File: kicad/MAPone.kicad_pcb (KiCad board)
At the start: 2 copper layers, 0 parts

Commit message: MAPone schematic, work in progress
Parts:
- added C1: 100n, Capacitors_ThroughHole:Capacitor7x2RM5, F.Cu at (206.5, 134.9)
- added C2: 100u, Capacitors_ThroughHole:Capacitor5x6RM2.5, F.Cu at (207.7, 115.4)
- added C3: 100n, Capacitors_ThroughHole:Capacitor7x2RM5, F.Cu at (233.5, 119.8)
- added C4: 100n, Capacitors_ThroughHole:Capacitor7x2RM5, F.Cu at (214.8, 138.6)
- added C5: 100n, Capacitors_ThroughHole:Capacitor7x2RM5, F.Cu at (225.2, 119.8)
- added C6: 100n, Capacitors_ThroughHole:Capacitor7x2RM5, F.Cu at (214.8, 129.5)
- added D1: D_CPL, Diodes_ThroughHole:Diode_DO-35_SOD27_Horizontal_RM10, F.Cu at (171.2, 141.3)
- added D2: PWR, LEDs:LED-5MM, F.Cu at (205.6, 125.4)
- added D3: Blink, LEDs:LED-5MM, F.Cu at (180.7, 140.8)
- added H1: V_SEL, Pin_Headers:Pin_Header_Straight_1x03, F.Cu at (196.3, 140.2)
- added H2: Power, Pin_Headers:Pin_Header_Straight_1x07, F.Cu at (195.2, 118.6)
- added H4: ANALOG, Pin_Headers:Pin_Header_Straight_1x06, F.Cu at (172.9, 124.0)
- added H5: AREF, Pin_Headers:Pin_Header_Straight_1x03, F.Cu at (188.0, 140.2)
- added H6: IO_L, Pin_Headers:Pin_Header_Straight_1x08, F.Cu at (214.5, 108.2)
- added H7: IO_H, Pin_Headers:Pin_Header_Straight_1x08, F.Cu at (175.5, 118.6)
- added H8: FTDI, Pin_Headers:Pin_Header_Straight_1x06, F.Cu at (188.8, 124.0)
- added H9: ISP, Pin_Headers:Pin_Header_Straight_2x03, F.Cu at (223.2, 129.9)
- added R1: 10k, Resistors_ThroughHole:Resistor_Horizontal_RM10mm, F.Cu at (231.3, 109.8)
- added R2: 1k, Resistors_ThroughHole:Resistor_Horizontal_RM10mm, F.Cu at (184.0, 130.8)
- added R3: 1k, Resistors_ThroughHole:Resistor_Horizontal_RM10mm, F.Cu at (171.3, 130.8)
- added U1: 7805, Discret:LM78XXV, F.Cu at (215.7, 119.8)
- added U2: ATMEGA328-P, Sockets_DIP:DIP-28__300_ELL, F.Cu at (184.5, 109.7)
- added X1: 16MHz, Crystals:Crystal_HC49-U_Vertical_3Pin, F.Cu at (196.3, 131.2)

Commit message: MAPone schematic, work in progress
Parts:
- added C7: 22pF, Discret:C1, F.Cu at (98.0, 86.0)
- added C8: 22pF, Discret:C1, F.Cu at (92.0, 86.0)
- added J1: BARREL_JACK, uControl:JACK_ALIM, F.Cu at (60.0, 115.0)
- added J2: USB-Micro, BADGEr:USB_B_Micro, F.Cu at (56.0, 104.0)
- added P1: CONN_1, BADGEr:vite_3mm, F.Cu at (77.0, 76.0)
- added P2: CONN_1, BADGEr:vite_3mm, F.Cu at (133.0, 76.0)
- added P3: CONN_1, BADGEr:vite_3mm, F.Cu at (78.0, 120.0)
- added P4: CONN_1, BADGEr:vite_3mm, F.Cu at (134.0, 119.0)
- added SW1: RST, uControl:SW-PB, F.Cu at (126.0, 99.0)
- C2: footprint Capacitors_ThroughHole:Capacitor5x6RM2.5 -> Capacitors_Elko_ThroughHole:Elko_vert_11.2x6.3mm_RM2.5
- D1: value D_CPL -> 1N4007
- H7: footprint Pin_Headers:Pin_Header_Straight_1x08 -> Pin_Headers:Pin_Header_Straight_1x10
- H8: footprint Pin_Headers:Pin_Header_Straight_1x06 -> BADGEr:Header_FTDI
- H9: footprint Pin_Headers:Pin_Header_Straight_2x03 -> BADGEr:Header_ICSP
- moved C3 170.7 mm to (64.0, 100.0)
- moved U1 163.1 mm to (55.0, 92.0), turned to 180 degrees
- moved C4 151.2 mm to (71.0, 92.0), turned to 90 degrees
- moved D2 148.7 mm to (63.0, 83.0), turned to 180 degrees
- moved H1 143.6 mm to (61.0, 92.0), turned to 270 degrees
- moved C2 143.0 mm to (65.0, 106.0), turned to 180 degrees
- moved C5 126.3 mm to (99.0, 114.0)
- moved R2 123.3 mm to (67.0, 92.0), turned to 270 degrees
- moved R1 121.7 mm to (111.0, 91.0)
- moved C6 115.2 mm to (109.0, 84.0)
- moved C1 110.8 mm to (99.0, 108.0)
- moved X1 109.0 mm to (95.0, 91.0), turned to 180 degrees
- moved D1 103.6 mm to (71.0, 115.0), turned to 90 degrees
- moved D3 100.0 mm to (84.0, 115.0)
- moved H6 99.5 mm to (120.0, 77.0), turned to 180 degrees
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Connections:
- X1 pad 3: (no net) -> GND

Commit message: MAPone schematic, work in progress
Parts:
- added SHIELD**: ARDUINO_SHIELD, MAPone.pretty:ARDUINO_UNO_SHIELD_2_040pins, F.Cu at (67.0, 125.0)
- moved H2 77.0 mm to (179.0, 118.0)
- moved H4 77.0 mm to (199.0, 118.0)
- moved P3 77.0 mm to (155.0, 119.0)
- moved P4 77.0 mm to (211.0, 118.0)
- moved H6 68.4 mm to (188.0, 70.0)
- moved H7 68.4 mm to (164.0, 70.0)
- moved P1 68.4 mm to (145.0, 69.0)
- moved P2 68.4 mm to (201.0, 69.0)
- moved D2 42.1 mm to (93.0, 112.5), turned to 270 degrees
- moved R2 32.6 mm to (88.0, 117.0)
- moved U1 25.5 mm to (73.5, 74.5), turned to 270 degrees
- moved H1 18.2 mm to (78.0, 98.5)
- moved J2 15.1 mm to (71.0, 106.0)
- moved H9 13.7 mm to (132.5, 96.5), turned to 270 degrees
- moved J1 12.0 mm to (72.0, 116.0)
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
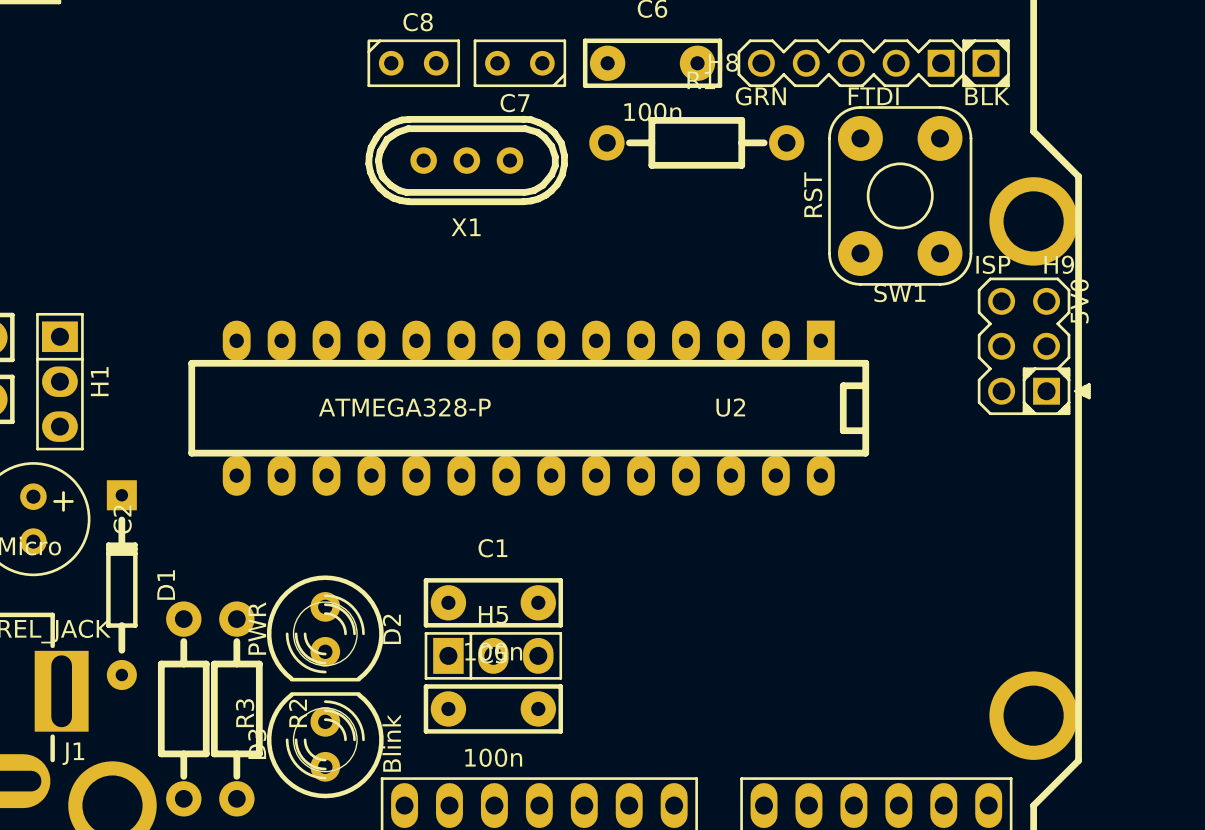
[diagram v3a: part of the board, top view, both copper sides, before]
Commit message: MAPone schematic review + PCB initialized
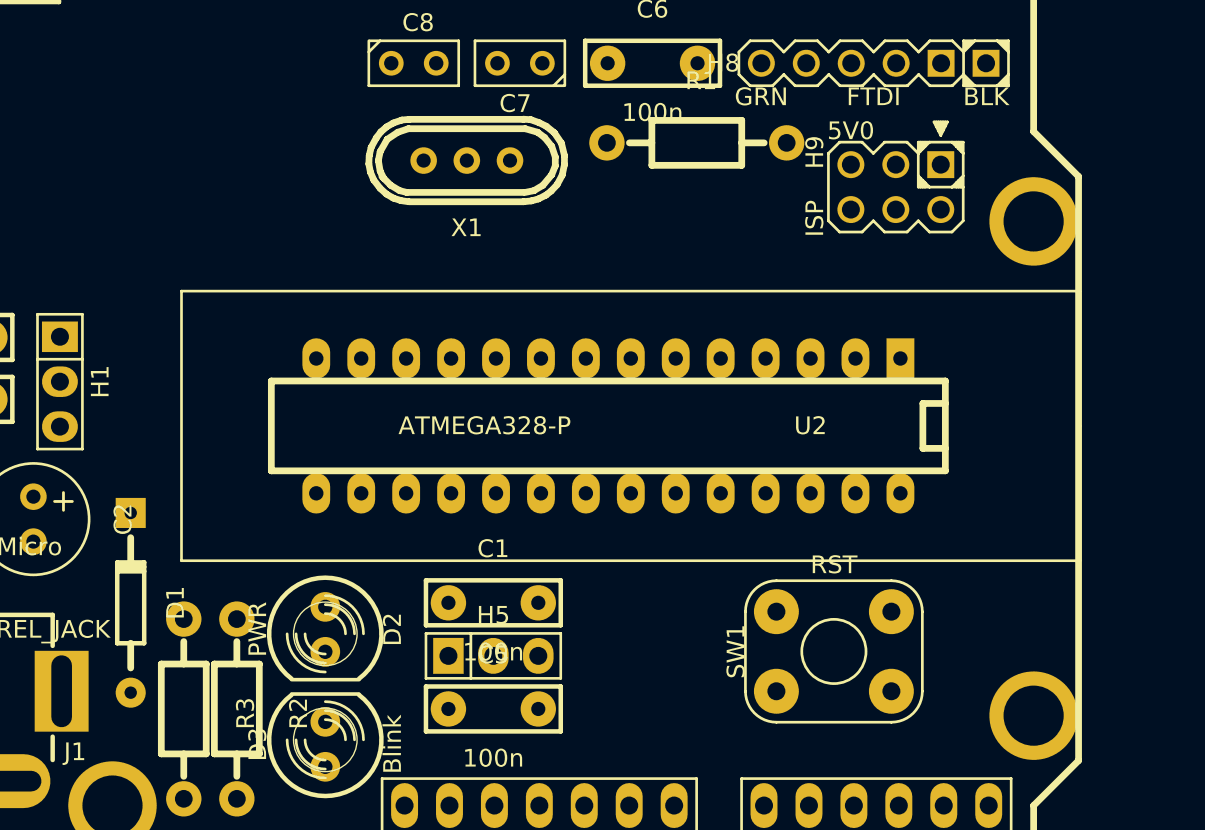
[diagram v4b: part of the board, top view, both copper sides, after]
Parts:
- U2: footprint Sockets_DIP:DIP-28__300_ELL -> MAPone.pretty:DIP-28__300_ELL_ZIF
- moved SW1 26.0 mm to (121.8, 113.8), turned to 90 degrees
- moved H9 11.6 mm to (125.2, 87.5), turned to 0 degrees
- moved U2 4.61 mm to (109.0, 101.0)
- moved D1 1.12 mm to (82.0, 111.0)

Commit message: MAPone PCB work in progress
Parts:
- removed P1, P2: CONN_1, BADGEr:vite_3mm
- removed SHIELD**: ARDUINO_SHIELD, MAPone.pretty:ARDUINO_UNO_SHIELD_2_040pins
- C1, C3, C4, C5, C6: footprint Capacitors_ThroughHole:Capacitor7x2RM5 -> MAPone.pretty:C_0805_HandSoldering; moved to B.Cu
- C2: footprint Capacitors_Elko_ThroughHole:Elko_vert_11.2x6.3mm_RM2.5 -> MAPone.pretty:Elko_vert_11.2x6.3mm_RM2.5
- C7, C8: footprint Discret:C1 -> MAPone.pretty:C_0805_HandSoldering; moved to B.Cu
- D1: footprint Diodes_ThroughHole:Diode_DO-35_SOD27_Horizontal_RM10 -> MAPone.pretty:Diode_DO-41_SOD81_Vertical_KathodeUp
- D2, D3: footprint LEDs:LED-5MM -> MAPone.pretty:LED-3MM
- H1: footprint Pin_Headers:Pin_Header_Straight_1x03 -> MAPone.pretty:Header_3
- H2: footprint Pin_Headers:Pin_Header_Straight_1x07 -> MAPone.pretty:Socket_Strip_Straight_1x06
- H4: footprint Pin_Headers:Pin_Header_Straight_1x06 -> MAPone.pretty:Socket_Strip_Straight_1x06
- H5: footprint Pin_Headers:Pin_Header_Straight_1x03 -> MAPone.pretty:Header_A_REF
- H6: footprint Pin_Headers:Pin_Header_Straight_1x08 -> MAPone.pretty:Socket_Strip_Straight_1x08
- H7: footprint Pin_Headers:Pin_Header_Straight_1x10 -> MAPone.pretty:Socket_Strip_Straight_1x08
- H8: footprint BADGEr:Header_FTDI -> MAPone.pretty:Header_FTDI
- H9: footprint BADGEr:Header_ICSP -> MAPone.pretty:Header_ICSP
- J1: footprint uControl:JACK_ALIM -> MAPone.pretty:JACK_ALIM
- J2: footprint BADGEr:USB_B_Micro -> MAPone.pretty:USB_B_Micro; moved to B.Cu
- P3, P4: footprint BADGEr:vite_3mm -> MAPone.pretty:vite_3mm
- R1, R2, R3: footprint Resistors_ThroughHole:Resistor_Horizontal_RM10mm -> MAPone.pretty:R_0805_HandSoldering; moved to B.Cu
- SW1: footprint uControl:SW-PB -> MAPone.pretty:SW-PB
- U1: footprint Discret:LM78XXV -> MAPone.pretty:LM78XXV
- X1: footprint Crystals:Crystal_HC49-U_Vertical_3Pin -> MAPone.pretty:Crystal_HC49-U_Vertical_3Pin
- moved H4 75.9 mm to (123.5, 110.0), turned to 180 degrees
- moved H2 73.6 mm to (105.8, 110.0)
- moved P3 71.4 mm to (84.0, 111.0)
- moved P4 71.3 mm to (140.0, 111.0)
- moved H6 68.6 mm to (121.0, 84.6), turned to 0 degrees
- moved H7 66.6 mm to (99.0, 84.6), turned to 180 degrees
- moved H9 32.6 mm to (92.7, 89.1)
- moved SW1 30.2 mm to (136.3, 87.3), turned to 270 degrees
- moved C6 27.8 mm to (131.3, 100.0)
- moved H5 27.8 mm to (114.6, 89.0)
- moved H8 25.2 mm to (140.0, 100.0), turned to 90 degrees
- moved C5 20.5 mm to (114.0, 100.0)
- moved C7 19.8 mm to (107.5, 100.0), turned to 0 degrees
- moved C8 19.8 mm to (101.3, 100.0), turned to 180 degrees
- moved R1 18.7 mm to (125.1, 100.1)
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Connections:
- H2 pad 1: /5V -> /RST
- H2 pad 2: /RST -> (no net)
- H2 pad 3: /3V3 -> /5V
- H2 pad 4: /5V -> GND
- H2 pad 6: GND -> /V_IN
- H8 pad 3: /V_USB -> /5V
- J1 pad 3: Net-(J1-Pad3) -> (no net)
- J2 pad 2: Net-(J2-Pad2) -> (no net)
- J2 pad 3: Net-(J2-Pad3) -> (no net)
- J2 pad 4: Net-(J2-Pad4) -> (no net)
- P3 pad 1: Net-(P3-Pad1) -> (no net)
- P4 pad 1: Net-(P4-Pad1) -> (no net)
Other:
- board outline added: 70 x 30 mm

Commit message: MAPone PCB work in progress
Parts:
- moved D1 1.95 mm to (83.5, 95.8)
- moved C3 0.63 mm to (78.0, 90.2)
- moved C4 0.56 mm to (81.0, 90.2)
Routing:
- net GND: track 0.00 -> 193.1 mm
- net /5V: track 0.00 -> 120.2 mm
- net /RST: track 0.00 -> 75.0 mm
- net /V_IN: track 0.00 -> 43.8 mm
- net /SCK: track 0.00 -> 40.1 mm
- net /MISO: track 0.00 -> 32.0 mm
- net /RXD: track 0.00 -> 31.8 mm
- net /PB1_P: track 0.00 -> 31.2 mm
- net /TXD: track 0.00 -> 30.2 mm
- net /SS_P: track 0.00 -> 26.7 mm
- net /MOSI_P: track 0.00 -> 25.8 mm
- net /V_USB: track 0.00 -> 22.2 mm
- net /PD5_P: track 0.00 -> 21.7 mm
- net /PD6_P: track 0.00 -> 21.6 mm
- net /PD7: track 0.00 -> 21.4 mm
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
